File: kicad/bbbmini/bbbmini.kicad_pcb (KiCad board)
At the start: 2 copper layers, 86.4 x 54.6 mm, 25 parts, among them P1 RC_OUTPUT, P10 GPS, P11 5V_INPUT, P12 SPI0, P13 CANBUS, P14 CANBUS R, P15 I2C2, P16 RC_1, P17 RC_3, P18 RC_4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

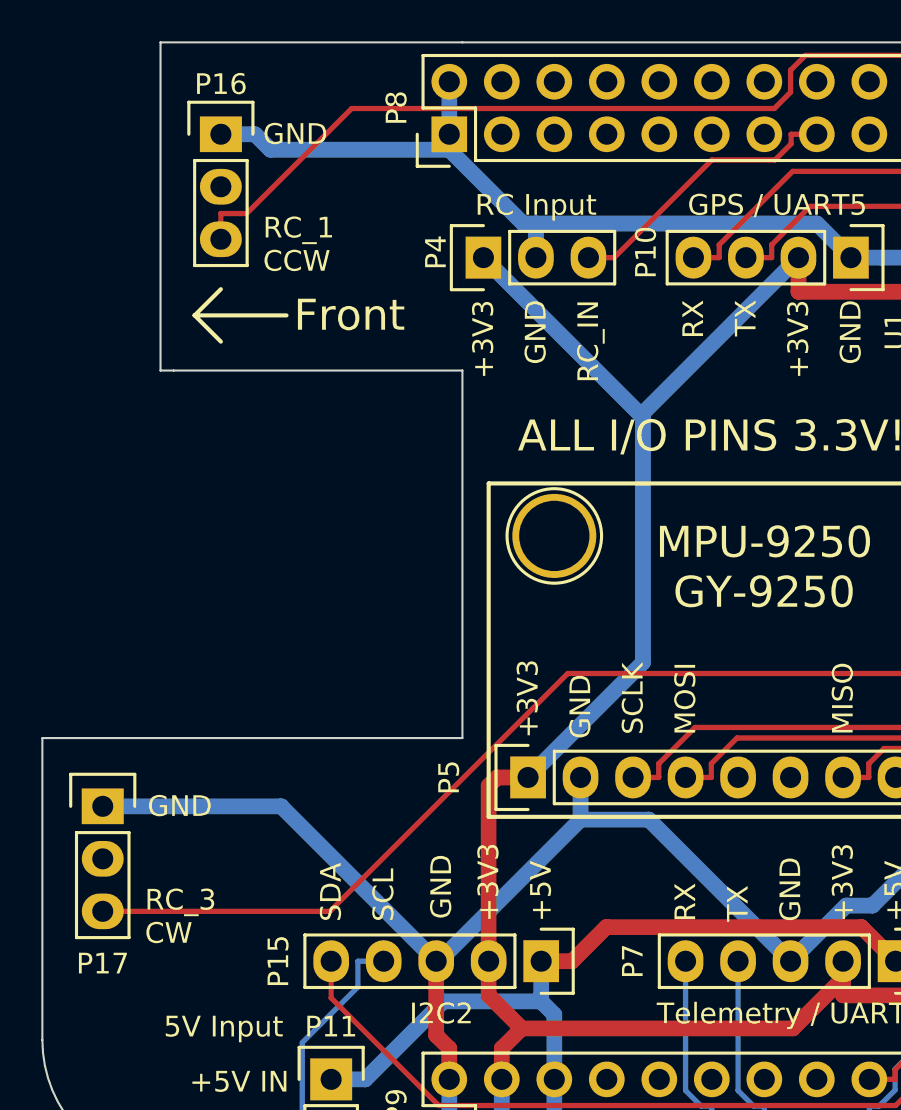
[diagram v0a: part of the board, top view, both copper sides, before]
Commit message: move RC_2 & RC_4 to reduce footprint and protect esc/servo cables using 90 degree pinheader
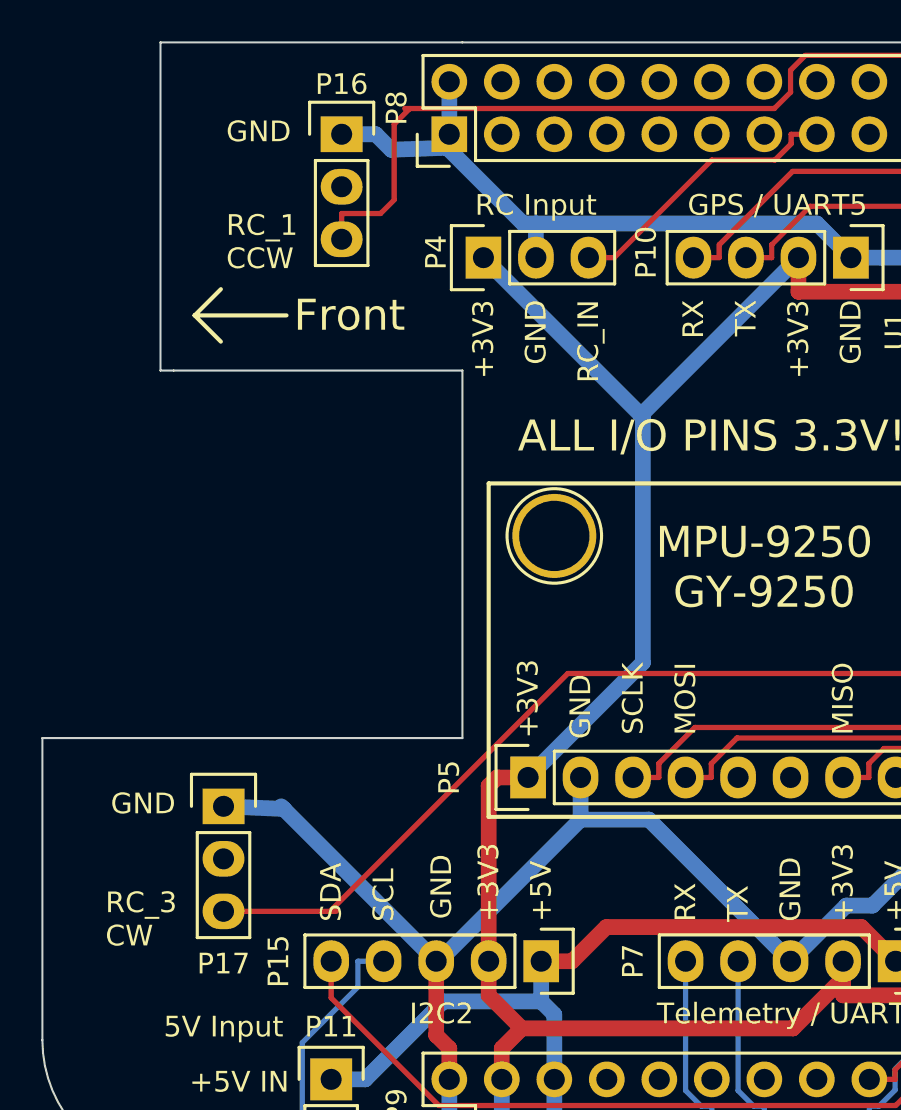
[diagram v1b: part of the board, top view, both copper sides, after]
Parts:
- moved P16 5.84 mm to (126.2, 79.4)
- moved P17 5.84 mm to (120.5, 111.9)
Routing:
- net GND: track 270.6 -> 259.5 mm
- net /RC_3: track 127.5 -> 122.0 mm
- net /RC_1: track 104.9 -> 101.5 mm
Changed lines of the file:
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@@
-(kicad_pcb (version 4) (host pcbnew 0.201505262310+5684~23~ubuntu14.04.1-product)
+(kicad_pcb (version 4) (host pcbnew 0.201507042246+5884~23~ubuntu14.04.1-product)
   (general
     (links 107)
-    (no_connects 0)
-    (area 111.709999 74.879999 198.170001 129.590001)
+    (no_connects 1)
+    (area 85.674287 41.6 228.015715 142.400001)
     (thickness 1.6)
     (drawings 110)
-    (tracks 444)
+    (tracks 448)
     (zones 0)
     (modules 25)
@@
   )
   (module Pin_Headers:Pin_Header_Straight_1x03 (layer F.Cu)
-    (at 120.396 79.375)
+    (at 126.238 79.375)
     (descr "Through hole pin header")
     (tags "pin header")
@@
   )
   (module Pin_Headers:Pin_Header_Straight_1x03 (layer F.Cu)
-    (at 114.681 111.887)
+    (at 120.523 111.887)
     (descr "Through hole pin header")
     (tags "pin header")
@@
     (effects (font (size 1 1) (thickness 0.2)) (justify left))
   )
-  (gr_text "RC_1\nCCW" (at 122.428 84.709) (layer F.SilkS)
-    (effects (font (size 1 1) (thickness 0.2)) (justify left))
-  )
-  (gr_text GND (at 122.428 79.375) (layer F.SilkS)
-    (effects (font (size 1 1) (thickness 0.2)) (justify left))
-  )
-  (gr_text "RC_3\nCW" (at 116.713 117.221) (layer F.SilkS)
-    (effects (font (size 1 1) (thickness 0.2)) (justify left))
-  )
-  (gr_text GND (at 116.84 111.887) (layer F.SilkS)
+  (gr_text "RC_1\nCCW" (at 120.65 84.582) (layer F.SilkS)
+    (effects (font (size 1 1) (thickness 0.2)) (justify left))
+  )
+  (gr_text GND (at 120.65 79.248) (layer F.SilkS)
+    (effects (font (size 1 1) (thickness 0.2)) (justify left))
+  )
+  (gr_text "RC_3\nCW" (at 114.808 117.348) (layer F.SilkS)
+    (effects (font (size 1 1) (thickness 0.2)) (justify left))
+  )
+  (gr_text GND (at 115.062 111.76) (layer F.SilkS)
     (effects (font (size 1 1) (thickness 0.2)) (justify left))
   )
@@
   (gr_line (start 111.76 123.19) (end 111.76 108.585) (angle 90) (layer Edge.Cuts) (width 0.1))
   (gr_arc (start 118.11 123.19) (end 118.11 129.54) (angle 90) (layer Edge.Cuts) (width 0.1))
+  (segment (start 127.4829 83.2101) (end 128.1179 83.2101) (width 0.254) (layer F.Cu) (net 1))
+  (segment (start 126.238 84.455) (end 126.238 83.2101) (width 0.254) (layer F.Cu) (net 1))
+  (segment (start 126.238 83.2101) (end 127.4829 83.2101) (width 0.254) (layer F.Cu) (net 1))
+  (segment (start 128.778 78.892) (end 129.54 78.13) (width 0.254) (layer F.Cu) (net 1))
+  (segment (start 128.778 82.55) (end 128.778 78.892) (width 0.254) (layer F.Cu) (net 1))
+  (segment (start 128.1179 83.2101) (end 128.778 82.55) (width 0.254) (layer F.Cu) (net 1))
+  (segment (start 129.286 78.13) (end 129.54 78.13) (width 0.254) (layer F.Cu) (net 1))
+  (segment (start 129.54 78.13) (end 147.1686 78.13) (width 0.254) (layer F.Cu) (net 1))
   (segment (start 163.2201 76.3192) (end 163.2201 76.835) (width 0.254) (layer F.Cu) (net 1))
   (segment (start 162.4605 75.5596) (end 163.2201 76.3192) (width 0.254) (layer F.Cu) (net 1))
@@
   (segment (start 147.955 77.3436) (end 147.955 76.2743) (width 0.254) (layer F.Cu) (net 1))
   (segment (start 147.1686 78.13) (end 147.955 77.3436) (width 0.254) (layer F.Cu) (net 1))
-  (segment (start 126.721 78.13) (end 147.1686 78.13) (width 0.254) (layer F.Cu) (net 1))
-  (segment (start 121.6409 83.2101) (end 126.721 78.13) (width 0.254) (layer F.Cu) (net 1))
-  (segment (start 120.396 83.2101) (end 121.6409 83.2101) (width 0.254) (layer F.Cu) (net 1))
-  (segment (start 120.396 84.455) (end 120.396 83.2101) (width 0.254) (layer F.Cu) (net 1))
   (segment (start 164.465 76.835) (end 163.2201 76.835) (width 0.254) (layer F.Cu) (net 1))
   (segment (start 189.2551 115.5951) (end 190.5 115.5951) (width 0.254) (layer B.Cu) (net 1))
@@
   (segment (start 189.8318 113.0551) (end 183.3041 106.5274) (width 0.254) (layer B.Cu) (net 2))
   (segment (start 190.5 113.0551) (end 189.8318 113.0551) (width 0.254) (layer B.Cu) (net 2))
+  (segment (start 120.523 116.967) (end 125.984 116.967) (width 0.254) (layer F.Cu) (net 3))
   (segment (start 167.005 76.835) (end 168.2499 76.835) (width 0.254) (layer F.Cu) (net 3))
   (segment (start 190.5 111.76) (end 190.5 110.5151) (width 0.254) (layer F.Cu) (net 3))
@@
   (segment (start 137.1758 105.4607) (end 183.0199 105.4607) (width 0.254) (layer F.Cu) (net 3))
   (segment (start 125.6695 116.967) (end 137.1758 105.4607) (width 0.254) (layer F.Cu) (net 3))
-  (segment (start 114.681 116.967) (end 125.6695 116.967) (width 0.254) (layer F.Cu) (net 3))
   (segment (start 188.0743 110.5151) (end 190.5 110.5151) (width 0.254) (layer F.Cu) (net 3))
   (segment (start 183.0199 105.4607) (end 188.0743 110.5151) (width 0.254) (layer F.Cu) (net 3))
@@
   (segment (start 167.64 110.49) (end 169.8871 108.2429) (width 0.762) (layer B.Cu) (net 13))
   (segment (start 131.445 79.375) (end 131.445 80.1244) (width 0.762) (layer B.Cu) (net 13))
-  (segment (start 120.396 79.375) (end 122.0473 79.375) (width 0.762) (layer B.Cu) (net 13))
+  (segment (start 126.238 79.375) (end 127.8893 79.375) (width 0.762) (layer B.Cu) (net 13))
   (segment (start 135.636 85.344) (end 135.636 83.6927) (width 0.762) (layer B.Cu) (net 13))
-  (segment (start 122.7967 80.1244) (end 122.0473 79.375) (width 0.762) (layer B.Cu) (net 13))
-  (segment (start 131.445 80.1244) (end 122.7967 80.1244) (width 0.762) (layer B.Cu) (net 13))
+  (segment (start 128.6387 80.1244) (end 127.8893 79.375) (width 0.762) (layer B.Cu) (net 13))
+  (segment (start 131.826 80.01) (end 128.6387 80.1244) (width 0.762) (layer B.Cu) (net 13))
   (segment (start 149.2247 83.6927) (end 135.636 83.6927) (width 0.762) (layer B.Cu) (net 13))
   (segment (start 150.876 85.344) (end 149.2247 83.6927) (width 0.762) (layer B.Cu) (net 13))
@@
   (segment (start 130.9439 119.38) (end 130.81 119.38) (width 0.762) (layer B.Cu) (net 13))
   (segment (start 137.795 112.5289) (end 130.9439 119.38) (width 0.762) (layer B.Cu) (net 13))
-  (segment (start 123.317 111.887) (end 114.681 111.887) (width 0.762) (layer B.Cu) (net 13))
+  (segment (start 123.444 112.014) (end 120.523 111.887) (width 0.762) (layer B.Cu) (net 13))
   (segment (start 130.81 119.38) (end 123.317 111.887) (width 0.762) (layer B.Cu) (net 13))
   (segment (start 135.89 119.38) (end 135.89 121.0313) (width 0.762) (layer B.Cu) (net 14))
